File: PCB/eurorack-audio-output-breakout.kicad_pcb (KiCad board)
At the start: 2 copper layers, 26.4 x 51.8 mm, 23 parts, among them J1 upper, J10 A, J11 B, J2 lower, J3 Conn_01x04_Pin, J4 Conn_01x02_Pin, J6 Conn_01x02_Pin, J7 Conn_01x02_Pin, J8 Conn_01x02_Pin, J9 Conn_01x02_Pin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

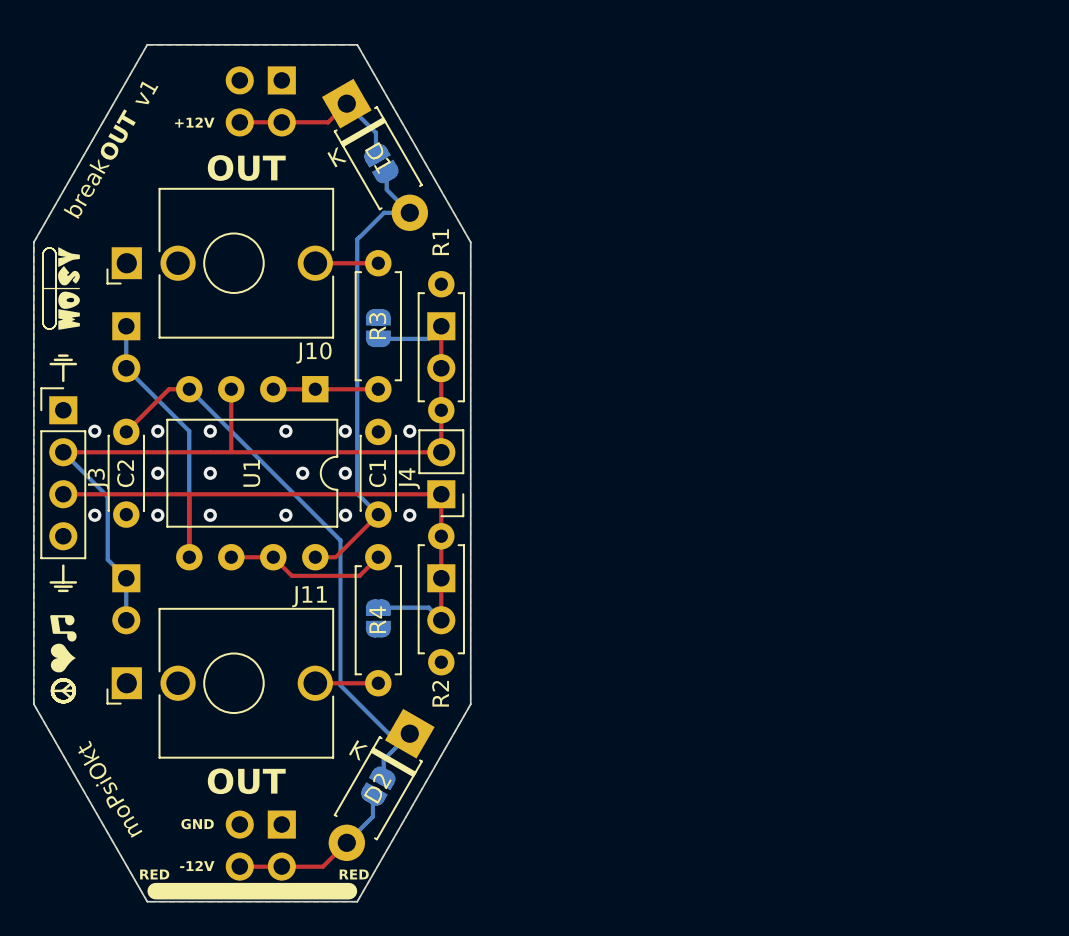
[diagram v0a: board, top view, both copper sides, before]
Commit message: Make the design slimmer
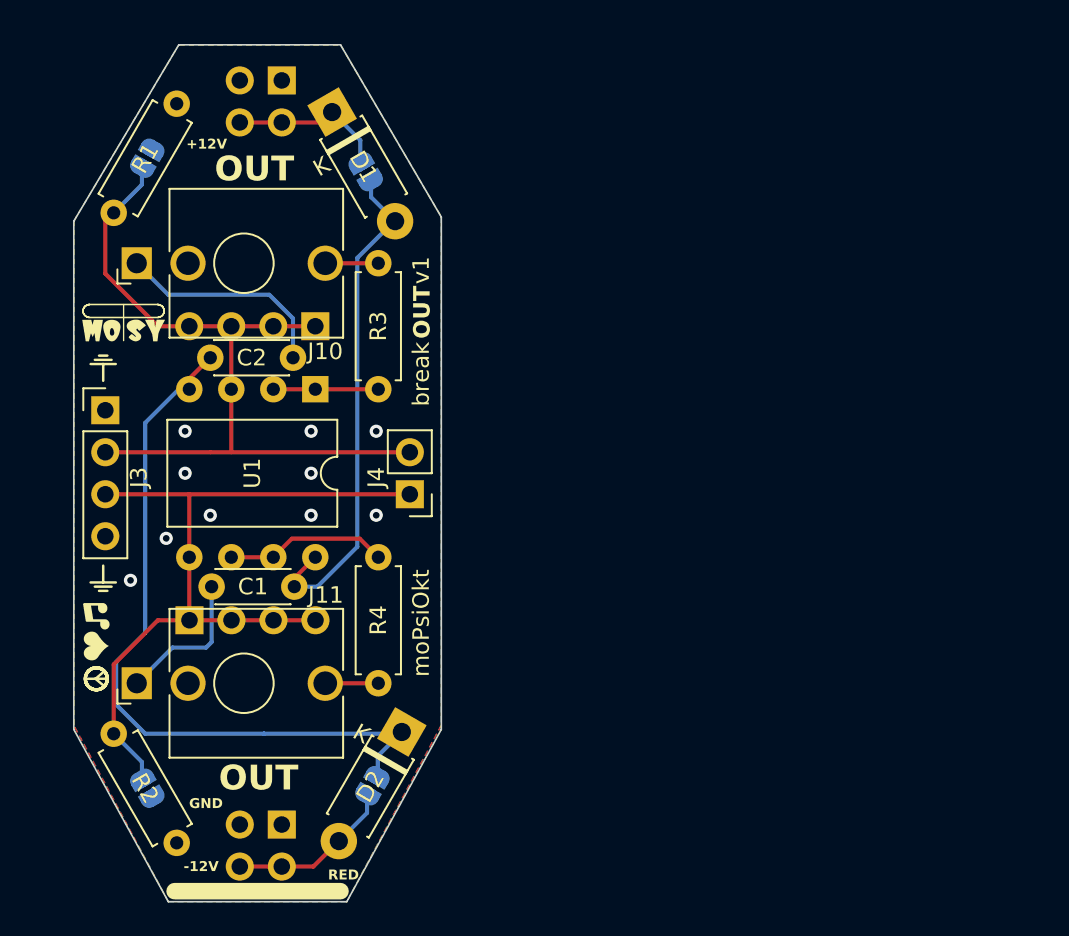
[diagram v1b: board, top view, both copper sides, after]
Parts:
- removed J6, J7, J8, J9: Conn_01x02_Pin, Connector_PinHeader_2.54mm:PinHeader_1x02_P2.54mm_Vertical
- added J12: Conn_01x04_Pin, Connector_PinHeader_2.54mm:PinHeader_1x04_P2.54mm_Vertical, B.Cu at (149.9, 99.1)
- added J5: Conn_01x04_Pin, Connector_PinHeader_2.54mm:PinHeader_1x04_P2.54mm_Vertical, B.Cu at (157.5, 81.3)
- moved R2 19.4 mm to (149.1, 112.5), turned to 120 degrees
- moved R1 19.4 mm to (149.1, 67.8), turned to -120 degrees
- moved JP4 17.3 mm to (147.3, 109.2), turned to 120 degrees
- moved JP3 17.3 mm to (147.3, 71.1), turned to -120 degrees
- moved C2 13.8 mm to (156.1, 83.2), turned to 180 degrees
- moved C1 6.69 mm to (156.2, 97.0), turned to 180 degrees
- moved J3 2.54 mm to (144.8, 86.4)
- moved J4 1.91 mm to (163.2, 91.4)
- moved JP1 1.06 mm to (160.5, 71.9)
- moved D1 1.02 mm to (158.5, 68.3)
- moved J10 0.60 mm to (153.2, 77.5)
- moved J11 0.60 mm to (153.2, 102.9)
- moved D2 0.49 mm to (162.7, 105.8)
- moved JP2 0.36 mm to (160.9, 109.1)
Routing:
- net GND: track 0.00 -> 22.1 mm, vias 16 -> 10
- net -12V: track 35.2 -> 47.1 mm
- net Net-(J12-Pin_1): track 54.0 -> 47.0 mm
- net Net-(J3-Pin_2): track 50.2 -> 47.2 mm
- net +12V: track 28.9 -> 30.8 mm
- net Net-(D1-K): track 10.7 -> 9.59 mm
- net Net-(J10-PadT): track 3.81 -> 3.21 mm
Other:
- board size 26.4 x 51.8 mm -> 22.2 x 51.8 mm
- board text added: "Audio Output"

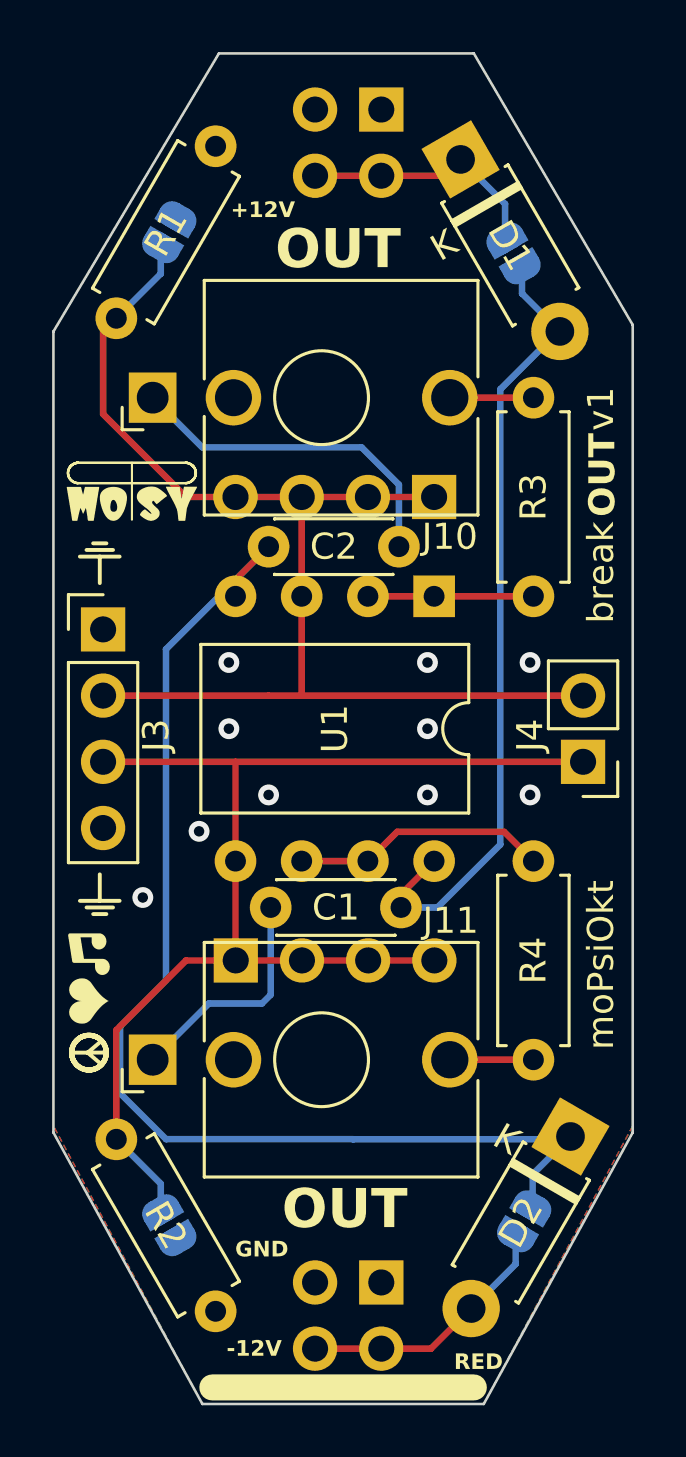
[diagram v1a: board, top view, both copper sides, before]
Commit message: Remove some components and make PCB slimmer
Reverse protection and pull-down are not really needed in a
breadboard environment, as component placement needs care and
focus anyways. Remove these components and make the PCB slimmer.
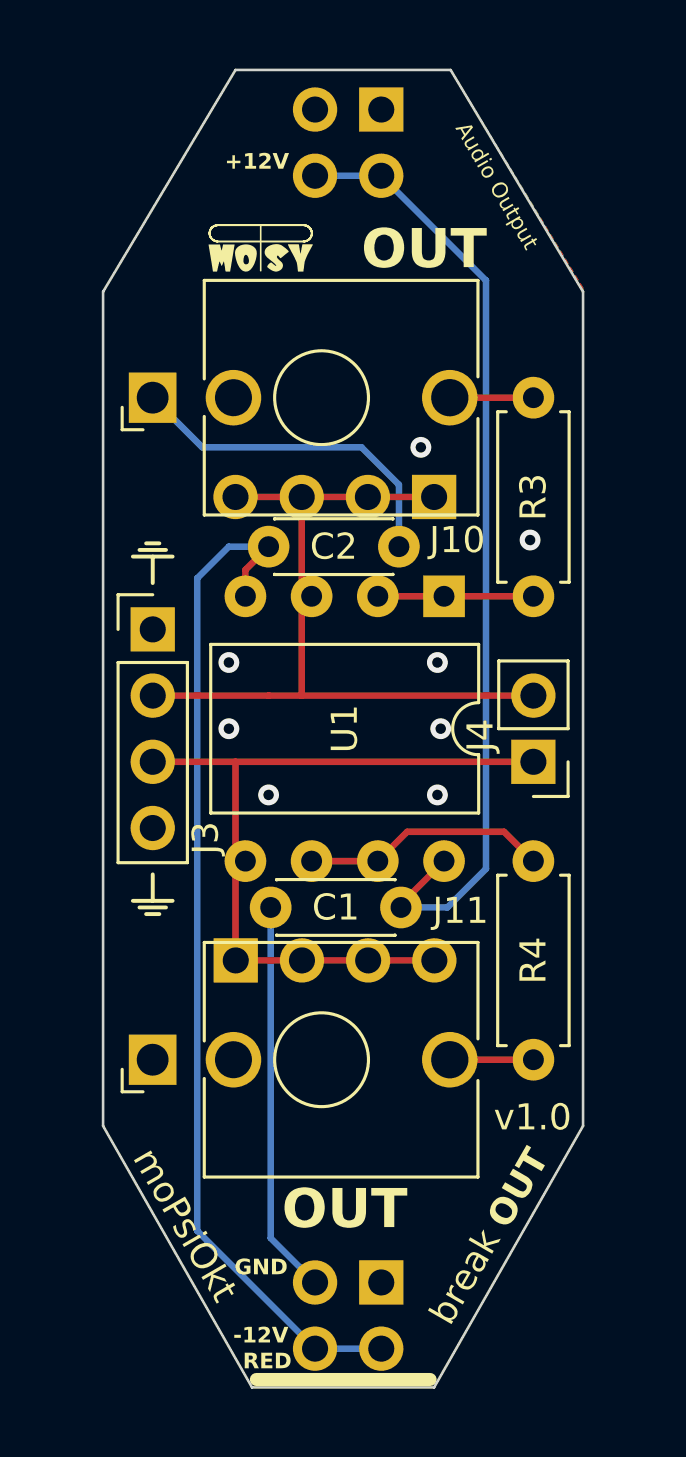
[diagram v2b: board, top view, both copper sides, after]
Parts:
- removed D1, D2: 1N5817, Diode_THT:D_DO-41_SOD81_P7.62mm_Horizontal
- removed JP1, JP2, JP3, JP4: SolderJumper_2_Open, Jumper:SolderJumper-2_P1.3mm_Open_RoundedPad1.0x1.5mm
- removed R1, R2: 1M, Resistor_THT:R_Axial_DIN0207_L6.3mm_D2.5mm_P7.62mm_Horizontal
- moved J3 1.91 mm to (146.7, 86.4)
- moved J4 1.91 mm to (161.3, 91.4)
- moved U1 0.38 mm to (157.9, 85.1)
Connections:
- J1 pad 3: Net-(D1-K) -> +12V
- J1 pad 4: Net-(D1-K) -> +12V
- J2 pad 3: Net-(D2-A) -> -12V
- J2 pad 4: Net-(D2-A) -> -12V
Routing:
- net Net-(J3-Pin_2): track 47.2 -> 30.2 mm
- net Net-(J12-Pin_1): track 47.0 -> 30.2 mm
- net Net-(D2-A): track 10.1 -> 0.00 mm
- net Net-(D1-K): track 9.59 -> 0.00 mm
- net -12V: track 47.1 -> 39.5 mm
- net +12V: track 30.8 -> 37.1 mm
- net GND: track 22.1 -> 28.3 mm, vias 10 -> 8
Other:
- board size 22.2 x 51.8 mm -> 18.4 x 50.5 mm
- board text added: "mopsy-music.de"
- board text added: "v1.0"
- board text removed: "v1"

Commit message: Change spelling of "moPsiOct"
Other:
- board text added: "moPsiOct"
- board text removed: "moPsiOkt"
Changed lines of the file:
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@@
     (effects (font (size 1 1) (thickness 0.2) bold) (justify left bottom))
   )
-  (gr_text "moPsiOkt" (at 145.796 106.68 -60) (layer "F.SilkS")
+  (gr_text "moPsiOct" (at 145.796 106.68 300) (layer "F.SilkS")
     (effects (font (size 1 1) (thickness 0.15)) (justify left bottom))
   )

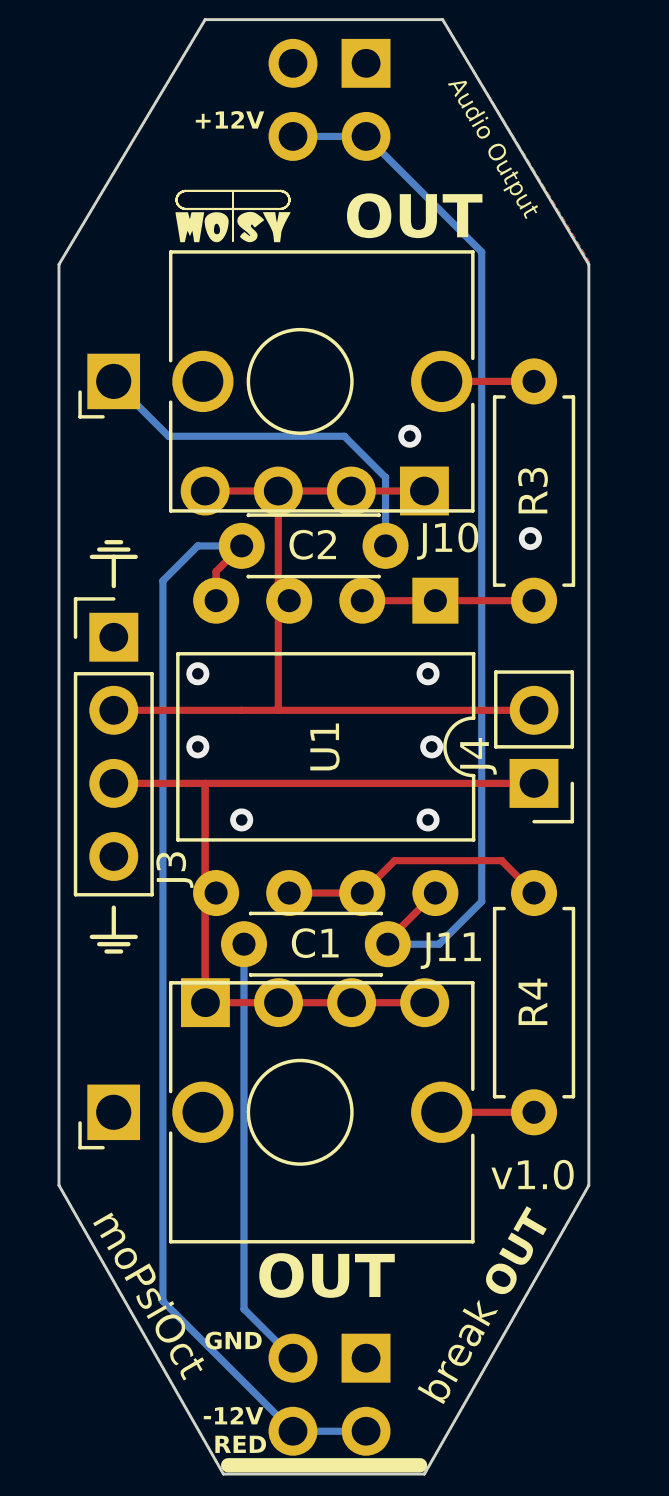
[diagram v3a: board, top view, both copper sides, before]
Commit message: Add A/B designators to the two channels
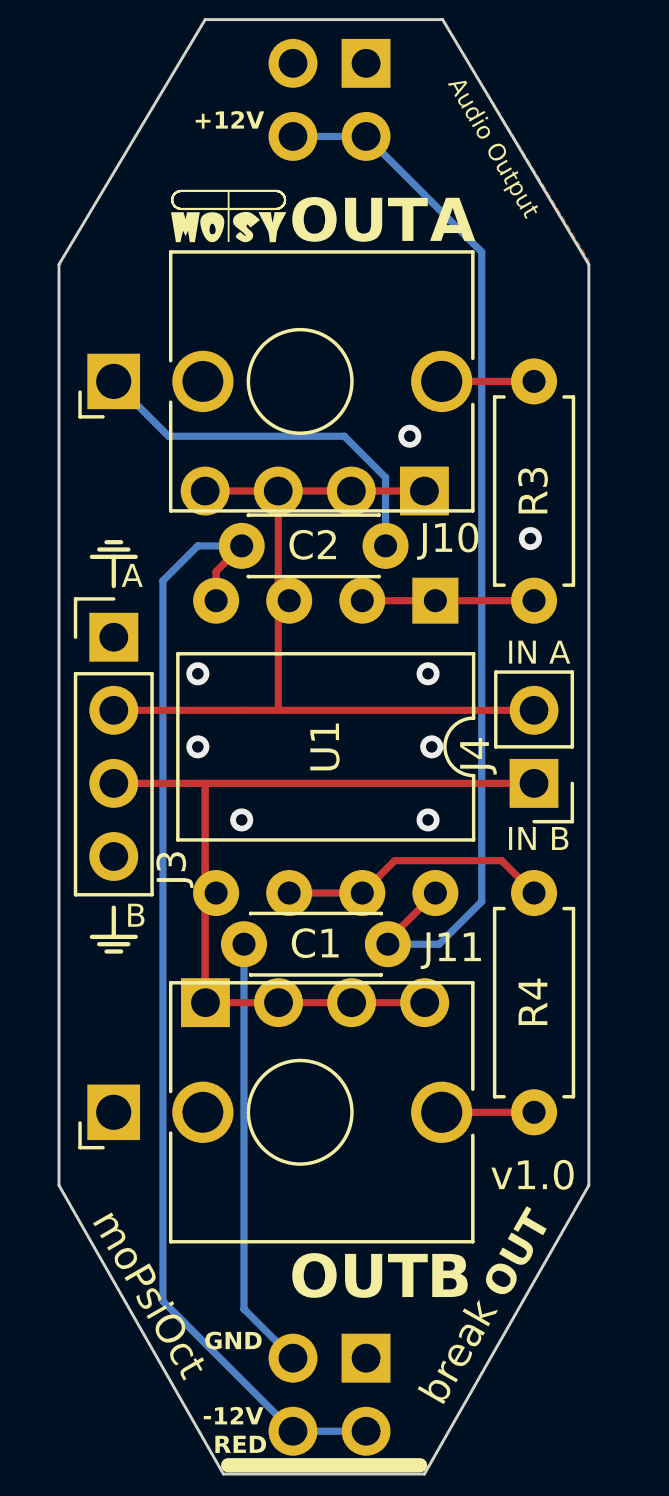
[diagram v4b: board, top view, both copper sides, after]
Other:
- board text added: "A"
- board text added: "B"
- board text added: "IN A"
- board text added: "IN B"

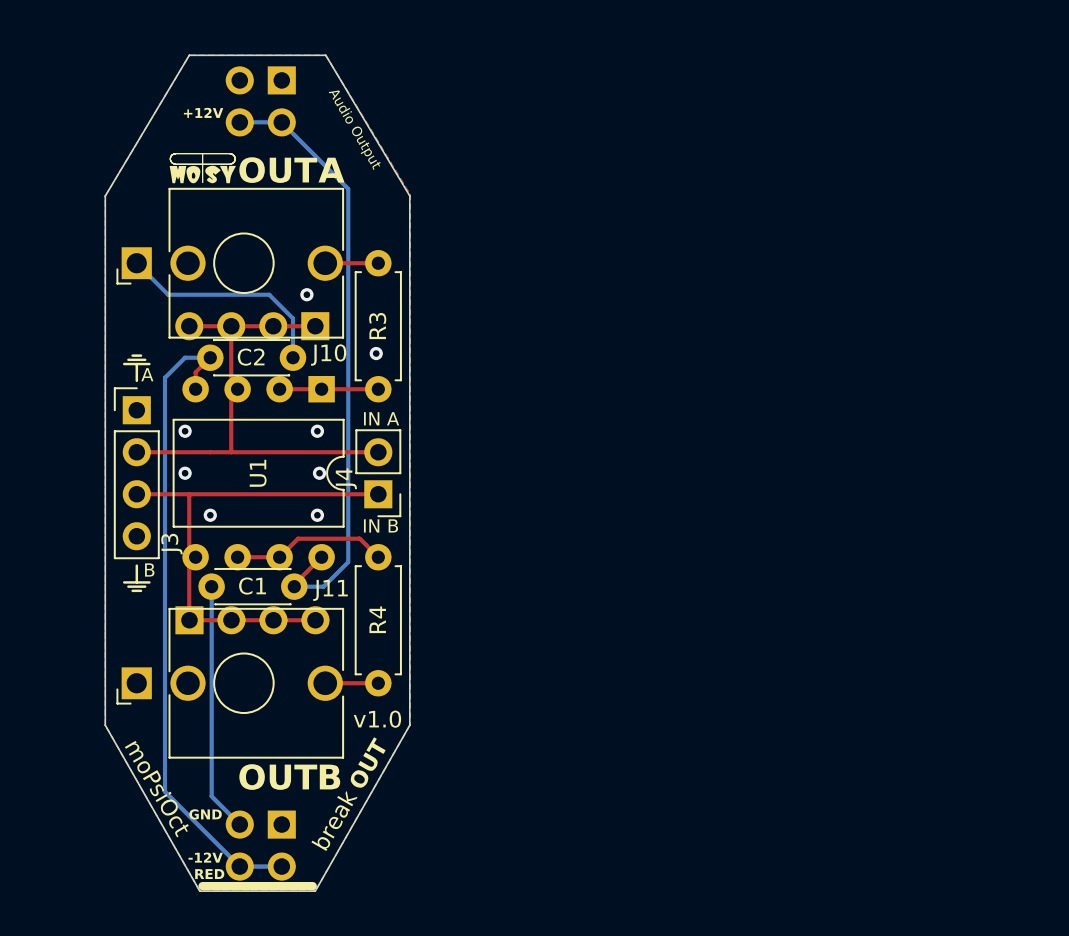
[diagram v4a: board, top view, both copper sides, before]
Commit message: Use part for breadboard power and fix spacing
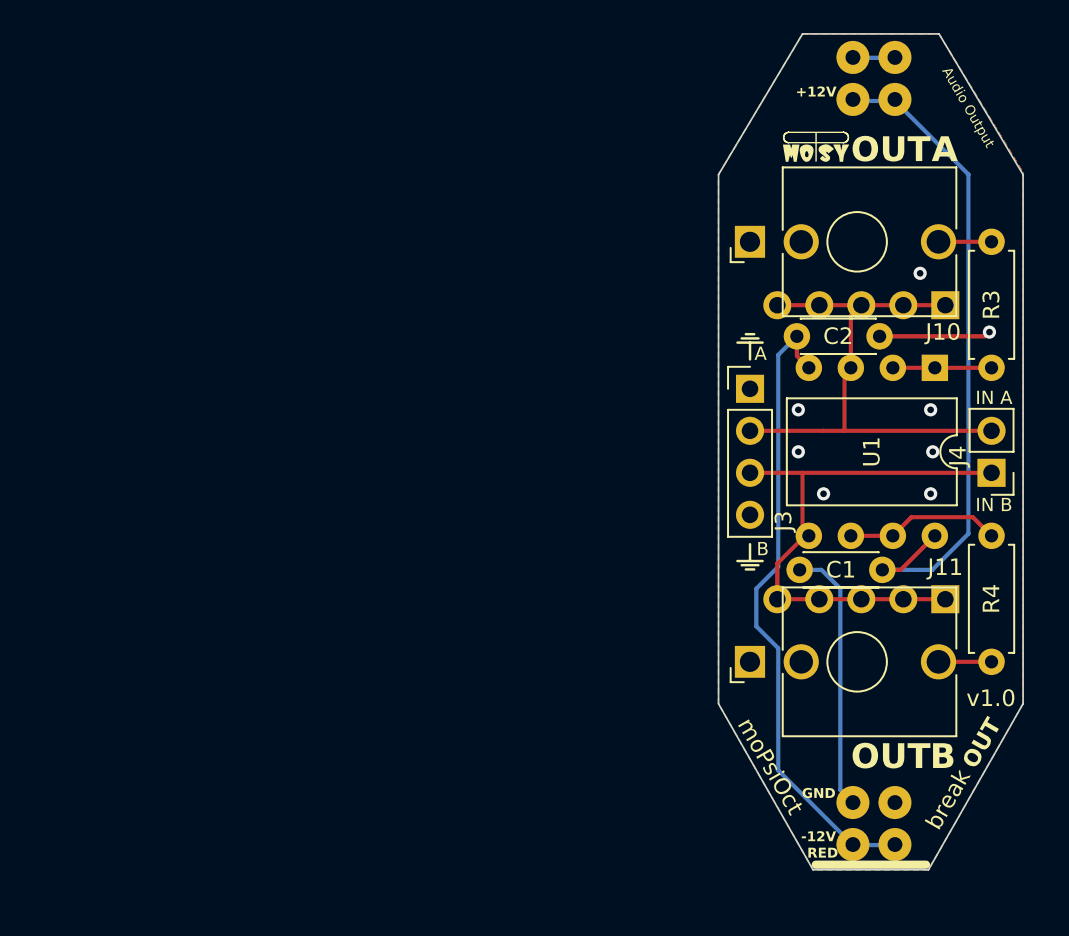
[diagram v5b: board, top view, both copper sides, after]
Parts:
- removed J2: lower, Connector_PinHeader_2.54mm:PinHeader_2x02_P2.54mm_Vertical
- J1: value upper -> Conn_01x04_Pin; footprint Connector_PinHeader_2.54mm:PinHeader_2x02_P2.54mm_Vertical -> moPsy:Breadboard Power Connector
- J12, J5: value Conn_01x04_Pin -> Conn_01x05_Pin; footprint Connector_PinHeader_2.54mm:PinHeader_1x04_P2.54mm_Vertical -> Connector_PinHeader_2.54mm:PinHeader_1x05_P2.54mm_Vertical
- moved J12 45.7 mm to (195.6, 97.8), turned to 90 degrees
- moved J1 42.9 mm to (192.0, 88.8)
- moved J5 38.1 mm to (195.6, 80.0)
- moved J10 37.1 mm to (190.2, 76.2)
- moved J11 37.1 mm to (190.2, 101.6)
- moved J3 37.1 mm to (183.8, 85.1)
- moved J4 37.1 mm to (198.4, 90.1)
- moved R3 37.1 mm to (198.4, 83.8)
- moved R4 37.1 mm to (198.4, 94.0)
- moved U1 37.1 mm to (194.9, 83.8)
- moved C1 35.6 mm to (191.8, 96.0)
- moved C2 35.5 mm to (191.6, 81.9)
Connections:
- J1 pad 2: unconnected-(J1-Pin_2-Pad2) -> +12V
- J1 pad 3: +12V -> GND
- J1 pad 4: +12V -> -12V
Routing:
- net GND: track 28.3 -> 23.0 mm
- net +12V: track 37.1 -> 40.7 mm
- net Net-(J12-Pin_1): track 30.2 -> 33.5 mm
- net Net-(J3-Pin_2): track 30.2 -> 32.8 mm
- net unconnected-(J1-Pin_1-Pad1): track 0.00 -> 2.54 mm
- net -12V: track 39.5 -> 39.0 mm
